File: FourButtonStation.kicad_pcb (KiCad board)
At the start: 2 copper layers, 100 x 67 mm, 39 parts, among them J1 c8-inlet, J2 Conn_WallSocket, J3 I2C, J4 AVOX Adapter, J5 Conn_WallSocket, J6 USB_B_Micro, J7 Conn_WallSocket, J8 Conn_WallSocket, J9 I2C, K1 G5Q-1, K2 G5Q-1, K4 FINDER-36.11, K5 G5Q-1, Q1 MMBT3904, Q2 MMBT3904, Q3 MMBT3904, Q4 MMBT3904, Q5 MMBT3904, Q6 MMBT3904, SW3 RST, SW4 Boot, U1 CH340C, U2 radio-receiver, U3 ESP-07

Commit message: Schematic and routing
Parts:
- removed C1: TODO: 20u as SMD Package?, Capacitor_THT:CP_Radial_D5.0mm_P2.50mm
- removed D1: TODO: SMD Diodes Package, Diode_THT:D_DO-15_P2.54mm_Vertical_KathodeUp
- removed D2, D3, D4: D_Small, Diode_THT:D_DO-15_P2.54mm_Vertical_KathodeUp
- removed K5: G5Q-1, omron-g5sb-14:RELAY_G5SB-14_OMR
- removed Q2, Q4, Q5, Q6: MMBT3904, jlc_footprints:SOT-23-3_L2.9-W1.3-P1.90-LS2.4-BR
- removed SW3: RST, jlc_footprints:SW-SMD_4P-L5.1-W5.1-P3.70-LS6.5-TL-2
- removed SW4: Boot, jlc_footprints:SW-SMD_4P-L5.1-W5.1-P3.70-LS6.5-TL-2
- added J10: AC IN, TerminalBlock_Phoenix:TerminalBlock_Phoenix_MKDS-1,5-2_1x02_P5.00mm_Horizontal, F.Cu at (117.8, 138.2)
- added K3: G5LE-1, Relay_THT:Relay_SPDT_Omron-G5LE-1, F.Cu at (60.0, 122.0)
- added LED1: KT-0603R, jlc_footprints:LED0603-RD, F.Cu at (22.3, 117.3)
- added LED2: KT-0603R, jlc_footprints:LED0603-RD, F.Cu at (39.0, 117.3)
- added LED3: KT-0603R, jlc_footprints:LED0603-RD, F.Cu at (57.0, 117.3)
- added LED4: KT-0603R, jlc_footprints:LED0603-RD, F.Cu at (73.5, 117.3)
- added R10: 33k, jlc_footprints:R0603, F.Cu at (82.7, 117.2)
- added R2: 12k, jlc_footprints:R0402, F.Cu at (37.4, 102.5)
- added R3: 12k, jlc_footprints:R0402, F.Cu at (34.1, 105.6)
- added R7: 1k, jlc_footprints:R0603, F.Cu at (58.8, 117.3)
- added R8: 33k, jlc_footprints:R0603, F.Cu at (66.2, 117.2)
- added R9: 1k, jlc_footprints:R0603, F.Cu at (75.3, 117.3)
- added SW1: POWER, as12ap:as12ap, F.Cu at (81.7, 93.7)
- added SW2: RST, jlc_footprints:SW-SMD_4P-L5.1-W5.1-P3.70-LS6.5-TL-2, F.Cu at (74.8, 96.8)
- added SWe: Mode, jlc_footprints:SW-SMD_4P-L5.1-W5.1-P3.70-LS6.5-TL-2, F.Cu at (74.8, 106.2)
- added U10: SM4007PL, jlc_footprints:SOD-123F_L2.8-W1.8-LS3.7-RD, F.Cu at (70.8, 116.8)
- added U11: D882_C9634, jlc_footprints:SOT-89-3_L4.5-W2.5-P1.50-LS4.2-BR, F.Cu at (79.6, 116.5)
- added U4: SM4007PL, jlc_footprints:SOD-123F_L2.8-W1.8-LS3.7-RD, F.Cu at (19.5, 116.8)
- added U5: D882_C9634, jlc_footprints:SOT-89-3_L4.5-W2.5-P1.50-LS4.2-BR, F.Cu at (28.4, 116.5)
- added U6: SM4007PL, jlc_footprints:SOD-123F_L2.8-W1.8-LS3.7-RD, F.Cu at (36.3, 116.8)
- added U7: D882_C9634, jlc_footprints:SOT-89-3_L4.5-W2.5-P1.50-LS4.2-BR, F.Cu at (45.1, 116.5)
- added U8: SM4007PL, jlc_footprints:SOD-123F_L2.8-W1.8-LS3.7-RD, F.Cu at (54.3, 116.8)
- added U9: D882_C9634, jlc_footprints:SOT-89-3_L4.5-W2.5-P1.50-LS4.2-BR, F.Cu at (63.1, 116.5)
- J1: value c8-inlet -> AC IN
- J2: value Conn_WallSocket -> External 3V; footprint TerminalBlock_Phoenix:TerminalBlock_Phoenix_MKDS-1,5-2_1x02_P5.00mm_Horizontal -> Connector_PinHeader_2.54mm:PinHeader_1x02_P2.54mm_Vertical
- J3: value I2C -> TTL
- J4: value AVOX Adapter -> TODO: AVOX Adapter might need voltage divider
- J6: footprint Connector_USB:USB_Micro-B_Molex-105017-0001 -> jlc_footprints:MICRO-USB-SMD_1050171001
- J9: value I2C -> Conn_WallSocket; footprint jlc_footprints:CONN-SMD_BM04B-SRSS-TB -> TerminalBlock_Phoenix:TerminalBlock_Phoenix_MKDS-1,5-2_1x02_P5.00mm_Horizontal
- K1, K2: value G5Q-1 -> G5LE-1; footprint omron-g5sb-14:RELAY_G5SB-14_OMR -> Relay_THT:Relay_SPDT_Omron-G5LE-1
- K4: value FINDER-36.11 -> G5LE-1; footprint omron-g5sb-14:RELAY_G5SB-14_OMR -> Relay_THT:Relay_SPDT_Omron-G5LE-1
- R1: footprint Resistor_SMD:R_0603_1608Metric_Pad0.98x0.95mm_HandSolder -> jlc_footprints:R0603
- R4, R5: value TODO: 33k needs to be JLC Package -> 1k; footprint Resistor_SMD:R_0603_1608Metric_Pad0.98x0.95mm_HandSolder -> jlc_footprints:R0603
- R6: value TODO: 33k needs to be JLC Package -> 33k; footprint Resistor_SMD:R_0603_1608Metric_Pad0.98x0.95mm_HandSolder -> jlc_footprints:R0603
- moved R4 204.3 mm to (24.0, 117.3), turned to 90 degrees
- moved H4 193.3 mm to (21.1, 94.5)
- moved R5 187.9 mm to (40.8, 117.3), turned to 90 degrees
- moved H3 186.0 mm to (21.2, 148.2)
- moved R6 180.0 mm to (48.2, 117.2), turned to -90 degrees
- moved R1 161.7 mm to (31.5, 117.2), turned to -90 degrees
- moved J4 127.2 mm to (68.2, 95.7)
- moved Q3 113.5 mm to (35.0, 102.3), turned to -90 degrees
- moved Q1 113.2 mm to (36.5, 105.8), turned to 90 degrees
- moved H2 96.1 mm to (117.8, 94.8)
- moved J9 88.3 mm to (72.2, 148.1)
- moved U2 73.3 mm to (87.0, 91.3)
- moved K1 62.4 mm to (26.0, 122.0)
- moved PS1 55.5 mm to (97.0, 140.0), turned to 90 degrees
- moved J5 45.2 mm to (29.8, 148.1)
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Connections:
- J2 pad 1: /AC2 -> GND
- J2 pad 2: /Nullleiter -> POWX
- J3 pad 2: +3V3 -> TX
- J3 pad 3: SDA -> RX
- J3 pad 4: SCL -> +3V3
- J4 pad 1: +3V3 -> GND
- J4 pad 2: GND -> ADC
- J4 pad 3: ADC -> +3V3
- J7 pad 1: /AC3 -> /AC2
- J8 pad 1: /AC4 -> /AC3
- J9 pad 1: GND -> /AC4
- J9 pad 2: +3V3 -> /Nullleiter
- K1 pad 1: Net-(D1-A) -> /Phase
- K1 pad 2: /Phase -> Net-(U4-A)
- K2 pad 1: Net-(D3-A) -> /Phase
- K2 pad 2: /Phase -> Net-(U6-A)
- K2 pad 3: /AC3 -> /AC2
- K4 pad 1: (no net) -> /Phase
- K4 pad 2: (no net) -> Net-(U10-A)
- K4 pad 3: (no net) -> /AC4
- K4 pad 4: (no net) -> unconnected-(K4-Pad4)
- PS1 pad 4: +3V3 -> Net-(PS1-+Vo)
- R4 pad 1: Relay2 -> Net-(U4-A)
- R5 pad 1: Relay3 -> Net-(U6-A)
- R6 pad 1: Relay4 -> Relay2
- U3 pad 1: Net-(U3-~{RST}) -> RESET
- U3 pad 10: SCL -> RadioC
- U3 pad 11: RadioD -> RadioB
- U3 pad 12: Net-(U3-GPIO0) -> GPIO0
- U3 pad 13: RadioC -> RadioA
- U3 pad 15: TX -> RX
- U3 pad 16: RX -> TX
- U3 pad 7: SDA -> RadioD
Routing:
- net /Phase: track 0.00 -> 207.1 mm
- net /Nullleiter: track 0.00 -> 109.4 mm
- net RadioD: track 0.00 -> 70.6 mm, vias 0 -> 2
- net RESET: track 0.00 -> 57.3 mm, vias 0 -> 3
- net RadioB: track 0.00 -> 56.8 mm, vias 0 -> 2
- net RadioC: track 0.00 -> 56.1 mm, vias 0 -> 2
- net RadioA: track 0.00 -> 55.3 mm, vias 0 -> 2
- net GPIO0: track 0.00 -> 50.7 mm, vias 0 -> 4
- net Relay4: track 0.00 -> 49.9 mm, vias 0 -> 2
- net RX: track 0.00 -> 45.4 mm, vias 0 -> 2
- net TX: track 0.00 -> 44.9 mm, vias 0 -> 2
- net +3V3: track 0.00 -> 42.8 mm
- net Relay3: track 0.00 -> 36.3 mm, vias 0 -> 2
- net /AC_FUSE: track 0.00 -> 31.7 mm
- net GND: track 0.00 -> 27.8 mm, vias 0 -> 10
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- added copper zone on F.Cu, net +3V3
- added copper zone on B.Cu, net GND
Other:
- board size 100 x 67 mm -> 106 x 63.5 mm

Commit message: Prepare for production
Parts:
- removed SWe: Mode, jlc_footprints:SW-SMD_4P-L5.1-W5.1-P3.70-LS6.5-TL-2
- added C1: 10u, jlc_footprints:C0402, F.Cu at (29.8, 93.5)
- added C2: 100n, jlc_footprints:C0402, F.Cu at (28.4, 93.5)
- added C3: 22u, jlc_footprints:C0603, F.Cu at (26.9, 93.5)
- added C4: 100u, jlc_footprints:C1206, F.Cu at (28.6, 112.0)
- added C5: 100n, jlc_footprints:C0402, F.Cu at (39.1, 111.5)
- added C6: 10u, jlc_footprints:C0402, F.Cu at (38.0, 111.5)
- added R11: 22k, jlc_footprints:R0603, F.Cu at (70.0, 106.0)
- added R12: 10k, jlc_footprints:R0603, F.Cu at (70.0, 108.0)
- added SW5: Mode, jlc_footprints:SW-SMD_4P-L5.1-W5.1-P3.70-LS6.5-TL-2, F.Cu at (74.8, 105.0)
- added SYM1: SYM_Flash_XLarge, Symbol:Symbol_HighVoltage_Type2_CopperTop_VerySmall, B.Cu at (101.0, 129.5)
- added Sym2: github.com/besi/four-button-station, Symbol:OSHW-Symbol_6.7x6mm_SilkScreen, F.Cu at (64.5, 108.8)
- added U13: AMS1117-3_3, jlc_footprints:SOT-223-3_L6.5-W3.4-P2.30-LS7.0-BR, F.Cu at (33.7, 96.2)
- added kibuzzard-65EDF79E: G***, kibuzzard-65EDF79E, F.Cu at (117.0, 107.0)
- added kibuzzard-65EDF7BF: G***, kibuzzard-65EDF7BF, F.Cu at (95.0, 93.3)
- added kibuzzard-65EE2541: G***, kibuzzard-65EE2541, F.Cu at (58.0, 114.5)
- added kibuzzard-65EE2549: G***, kibuzzard-65EE2549, F.Cu at (39.5, 153.2)
- added kibuzzard-65EE2549: G***, kibuzzard-65EE2549, F.Cu at (40.0, 114.5)
- added kibuzzard-65EE2550: G***, kibuzzard-65EE2550, F.Cu at (25.0, 153.2)
- added kibuzzard-65EE2550: G***, kibuzzard-65EE2550, F.Cu at (23.0, 114.5)
- added kibuzzard-65EE2558: G***, kibuzzard-65EE2558, F.Cu at (74.5, 114.5)
- added kibuzzard-65EE261E: G***, kibuzzard-65EE261E, F.Cu at (82.8, 91.5)
- added kibuzzard-65EE2681: G***, kibuzzard-65EE2681, F.Cu at (81.2, 109.2)
- added kibuzzard-65EE2746: G***, kibuzzard-65EE2746, F.Cu at (66.0, 100.1)
- added kibuzzard-65EE278E: G***, kibuzzard-65EE278E, F.Cu at (117.5, 144.2)
- added kibuzzard-65EE27C8: G***, kibuzzard-65EE27C8, F.Cu at (82.0, 153.2)
- added kibuzzard-65EE27E0: G***, kibuzzard-65EE27E0, F.Cu at (67.2, 153.2)
- added kibuzzard-65EE2811: G***, kibuzzard-65EE2811, F.Cu at (22.2, 144.8)
- added kibuzzard-65EE298C: G***, kibuzzard-65EE298C, F.Cu at (83.5, 107.2)
- added kibuzzard-65EE35B8: G***, kibuzzard-65EE35B8, F.Cu at (71.0, 100.2)
- J3: value TTL -> UART
- J4: value TODO: AVOX Adapter might need voltage divider -> ADC
- moved H3 2.50 mm to (21.2, 150.8)
- moved J4 1.99 mm to (68.8, 97.6)
- moved J7 1.90 mm to (44.5, 149.8)
- moved J8 1.90 mm to (57.5, 149.8)
- moved SW1 1.85 mm to (81.7, 95.5)
- moved H2 1.80 mm to (119.2, 93.8)
- moved J9 1.75 mm to (72.2, 149.8)
- moved J5 1.66 mm to (29.8, 149.8)
- moved J3 1.62 mm to (63.8, 96.2)
- moved J2 1.60 mm to (81.2, 104.8)
- moved SW2 1.30 mm to (74.8, 95.5)
- moved H1 1.00 mm to (119.2, 150.8)
- moved H4 0.73 mm to (21.2, 93.8)
- moved J6 0.53 mm to (20.2, 103.2)
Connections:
- net POWX renamed POW3V3
- J10 pad 1: /Nullleiter -> /AC_FUSE
- J4 pad 2: ADC -> Net-(J4-Pin_2)
- J6 pad 1: VBUS -> +5V
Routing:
- net POW3V3: track 5.31 -> 68.4 mm, vias 0 -> 2
- net /Nullleiter: track 109.4 -> 89.3 mm
- net GND: track 27.8 -> 45.4 mm, vias 10 -> 21
- net TX: track 44.9 -> 54.4 mm, vias 2 -> 1
- net +3V3: track 42.8 -> 51.7 mm
- net RX: track 45.4 -> 54.0 mm, vias 2 -> 1
- net ADC: track 27.4 -> 34.4 mm, vias 1 -> 2
- net Net-(J4-Pin_2): track 0.00 -> 6.69 mm
- net +5V: track 0.00 -> 4.60 mm
- net Relay3: track 36.3 -> 40.6 mm
- net /Phase: track 207.1 -> 203.5 mm
- net /AC_FUSE: track 31.7 -> 35.1 mm
- net /AC1: track 15.9 -> 17.6 mm
- net RESET: track 57.3 -> 58.8 mm
- net /AC4: track 12.8 -> 14.2 mm
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- added copper zone on F.Cu, net +5V
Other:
- board size 106 x 63.5 mm -> 106 x 65 mm
- board text added: "JLCJLCJLCJLC"
- board text added: "Version 2.0 10.03.24 aabbccdd"

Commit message: Final tweaks
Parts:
- moved F1 1.42 mm to (110.0, 149.8)
- moved PS1 0.77 mm to (97.0, 140.8)
- moved SW2 0.75 mm to (74.8, 96.2)
- moved kibuzzard-65EDF7BF 0.66 mm to (95.0, 94.0)
- moved U2 0.65 mm to (87.0, 92.0)
- moved J10 0.50 mm to (117.2, 138.2)
- moved J1 0.25 mm to (120.0, 120.2)
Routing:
- net /AC_FUSE: track 35.1 -> 32.4 mm
- net GND: track 45.4 -> 44.2 mm
- net RESET: track 58.8 -> 58.0 mm
- net RadioD: track 71.4 -> 70.8 mm
- net RadioC: track 56.3 -> 55.6 mm
- net +3V3: track 51.7 -> 51.0 mm
- net RadioB: track 56.9 -> 56.2 mm
- net /Nullleiter: track 89.3 -> 88.7 mm
- net /Phase: track 203.5 -> 202.9 mm

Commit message: Production files for 2.0
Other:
- board text added: "Version 2.0 10.03.24 aa14c0f4"
- board text removed: "Version 2.0 10.03.24 aabbccdd"
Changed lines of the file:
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@@
   (gr_line (start 37.25 91.75) (end 37.25 94.75)
     (stroke (width 0.1) (type default)) (layer "Edge.Cuts"))
-  (gr_text "Version 2.0\n10.03.24\naabbccdd" (at 113 104) (layer "F.SilkS")
+  (gr_text "Version 2.0\n10.03.24\naa14c0f4" (at 113 104) (layer "F.SilkS")
     (effects (font (size 1 1) (thickness 0.15)) (justify left bottom))
   )

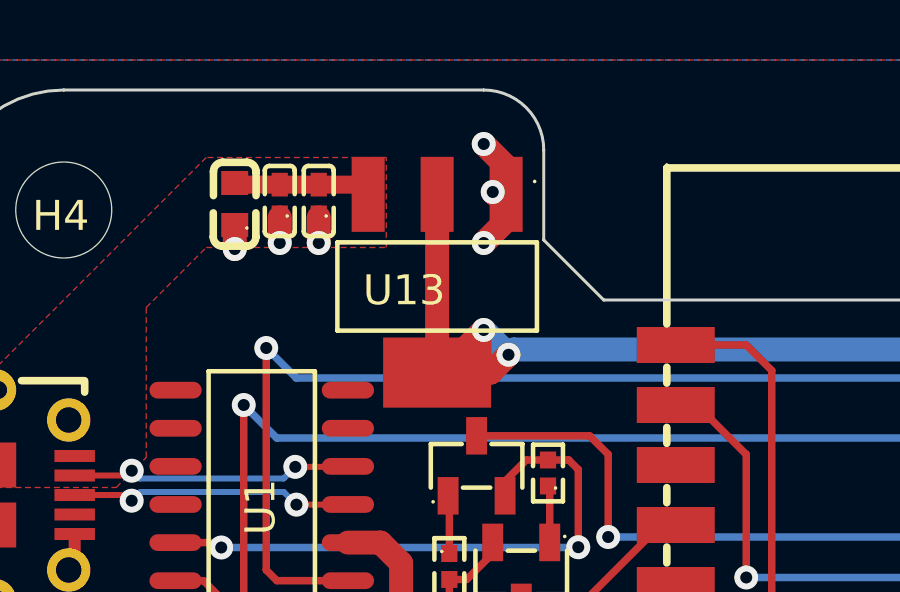
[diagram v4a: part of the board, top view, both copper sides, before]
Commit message: Thermal conductivity for the AMS117
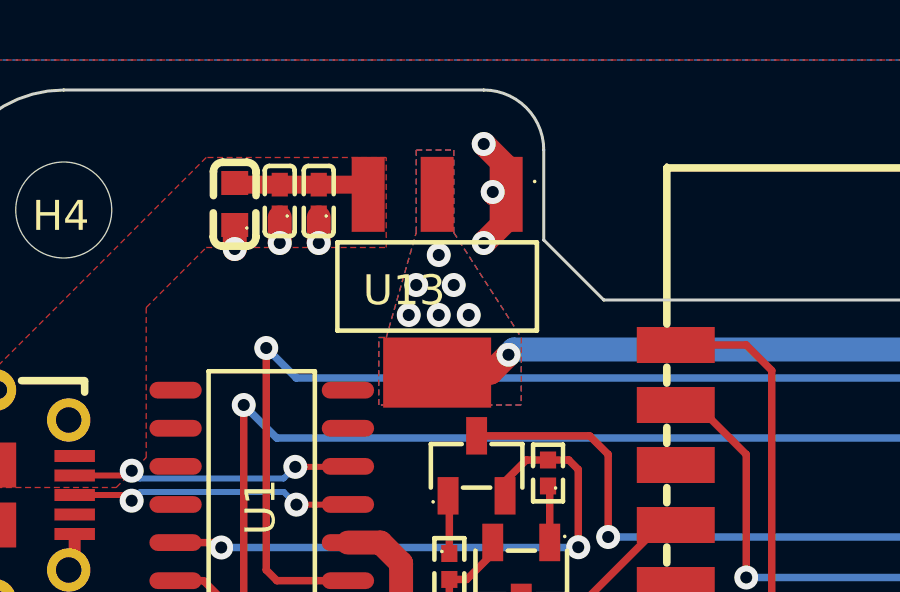
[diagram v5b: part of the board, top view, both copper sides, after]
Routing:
- net POW3V3: track 68.4 -> 59.3 mm, vias 2 -> 7
- added copper zone on B.Cu, net POW3V3
- added copper zone on F.Cu, net POW3V3
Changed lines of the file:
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@@
   (segment (start 83.75 104.71) (end 83.79 104.75) (width 0.8) (layer "F.Cu") (net 61))
   (segment (start 35.480949 99.169051) (end 36.075 98.575) (width 0.8) (layer "F.Cu") (net 61))
-  (segment (start 33.697116 93.229122) (end 33.697116 99.169051) (width 0.8) (layer "F.Cu") (net 61))
   (segment (start 82.83 100.58) (end 83.75 101.5) (width 0.8) (layer "F.Cu") (net 61))
-  (segment (start 33.830949 99.169051) (end 35.25 97.75) (width 0.8) (layer "F.Cu") (net 61))
   (segment (start 33.697116 99.169051) (end 35.480949 99.169051) (width 0.8) (layer "F.Cu") (net 61))
+  (via (at 33 96.25) (size 0.8) (drill 0.4) (layers "F.Cu" "B.Cu") (free) (net 61))
+  (via (at 33.75 97.25) (size 0.8) (drill 0.4) (layers "F.Cu" "B.Cu") (free) (net 61))
   (via (at 36.075 98.575) (size 0.8) (drill 0.4) (layers "F.Cu" "B.Cu") (net 61))
-  (via (at 35.25 97.75) (size 0.8) (drill 0.4) (layers "F.Cu" "B.Cu") (net 61))
+  (via (at 34.25 96.25) (size 0.8) (drill 0.4) (layers "F.Cu" "B.Cu") (free) (net 61))
+  (via (at 34.75 97.25) (size 0.8) (drill 0.4) (layers "F.Cu" "B.Cu") (free) (net 61))
+  (via (at 32.75 97.25) (size 0.8) (drill 0.4) (layers "F.Cu" "B.Cu") (free) (net 61))
+  (via (at 33.75 95.25) (size 0.8) (drill 0.4) (layers "F.Cu" "B.Cu") (free) (net 61))
   (segment (start 36.250001 98.399999) (end 36.075 98.575) (width 0.8) (layer "B.Cu") (net 61))
-  (segment (start 35.25 97.75) (end 36.075 98.575) (width 0.8) (layer "B.Cu") (net 61))
   (segment (start 60.518127 98.399999) (end 36.250001 98.399999) (width 0.8) (layer "B.Cu") (net 61))
   (segment (start 81.65 100.58) (end 78.58 100.58) (width 0.8) (layer "B.Cu") (net 61))
@@
   )
   (zone (net 59) (net_name "+5V") (layer "F.Cu") (name "5v") (hatch edge 0.5)
-    (priority 1)
+    (priority 3)
     (connect_pads yes (clearance 0.25))
     (min_thickness 0.25) (filled_areas_thickness no)
@@
     )
   )
+  (zone (net 0) (net_name "") (layers "F&B.Cu") (name "Keepout-antenna-zone") (hatch edge 0.5)
+    (connect_pads yes (clearance 0))
+    (min_thickness 0.25) (filled_areas_thickness no)
+    (keepout (tracks allowed) (vias allowed) (pads allowed) (copperpour not_allowed) (footprints allowed))
+    (fill (thermal_gap 0.5) (thermal_bridge_width 0.5))
+    (polygon
+      (pts
+        (xy 37.25 89.75)
+        (xy 37.25 97.75)
+        (xy 61.25 97.75)
+        (xy 61.25 89.75)
+      )
+    )
+  )
+  (zone (net 61) (net_name "POW3V3") (layers "F&B.Cu") (hatch edge 0.5)
+    (priority 4)
+    (connect_pads (clearance 0))
+    (min_thickness 0.25) (filled_areas_thickness no)
+    (fill yes (thermal_gap 0.1) (thermal_bridge_width 0.8))
+    (polygon
+      (pts
+        (xy 32 98)
+        (xy 33 94.5)
+        (xy 33 91.75)
+        (xy 34.25 91.75)
+        (xy 34.25 94.5)
+        (xy 36.5 98)
+        (xy 36.5 100.25)
+        (xy 31.75 100.25)
+        (xy 31.75 98)
+      )
+    )
+  )
   (zone (net 1) (net_name "GND") (layer "B.Cu") (hatch edge 0.5)
     (priority 2)
@@
         (xy 111.25 88.75)
         (xy 13.25 88.75)
-        (xy 13.25 115.5)
       )
     )

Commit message: Prepare release 2.0
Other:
- board text added: "Version 2.0 11.03.24 95fb5d44"
- board text removed: "Version 2.0 10.03.24 aa14c0f4"
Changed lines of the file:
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@@
   (gr_line (start 37.25 91.75) (end 37.25 94.75)
     (stroke (width 0.1) (type default)) (layer "Edge.Cuts"))
-  (gr_text "Version 2.0\n10.03.24\naa14c0f4" (at 113 104) (layer "F.SilkS")
+  (gr_text "Version 2.0\n11.03.24\n95fb5d44" (at 113 104) (layer "F.SilkS")
     (effects (font (size 1 1) (thickness 0.15)) (justify left bottom))
   )

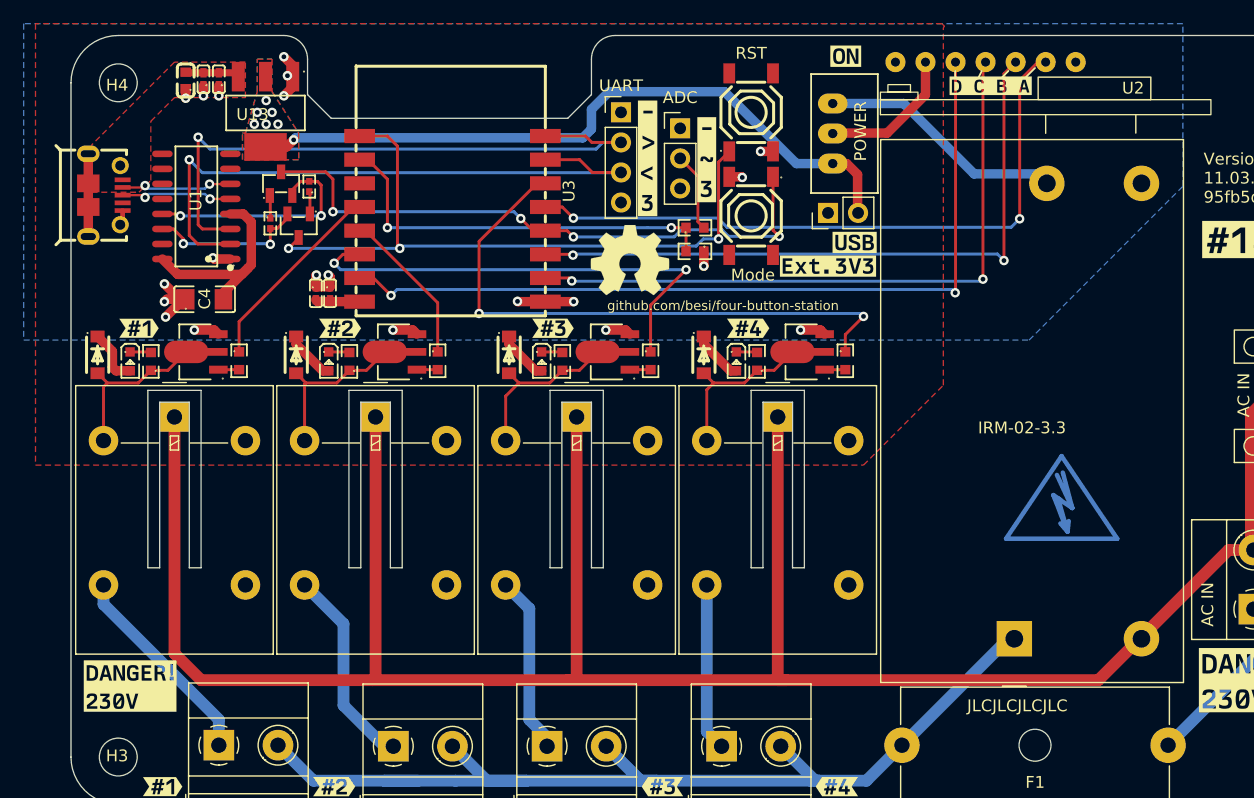
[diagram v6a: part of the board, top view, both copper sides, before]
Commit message: Update documentation and silkscreen
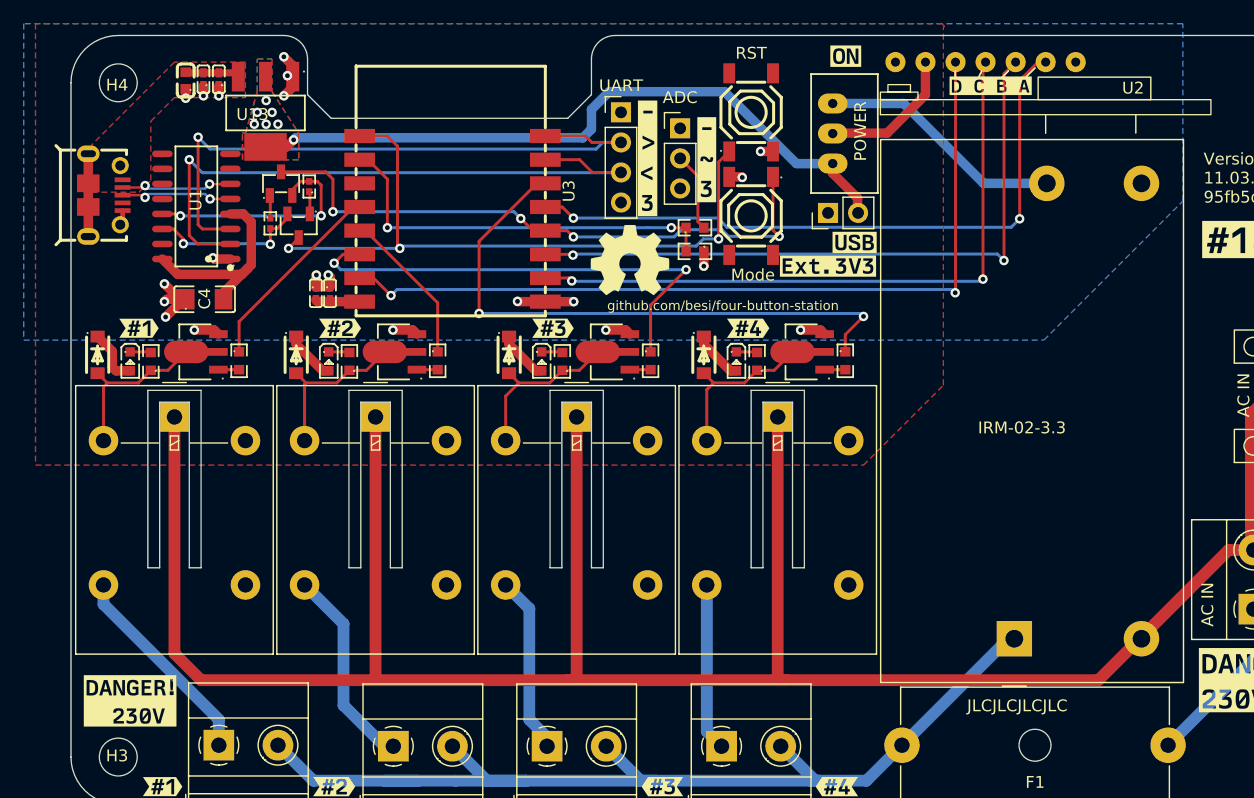
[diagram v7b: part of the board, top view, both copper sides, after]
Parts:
- removed the SYM1 at (101.0, 129.5)
- removed kibuzzard-65EE2811: G***, kibuzzard-65EE2811
- added G*** (x2): LOGO, LOGO, B.Cu at (76.8, 105.2)
- added G***: LOGO, LOGO, B.Cu at (29.8, 102.8)
- added SYM1: SYM_Flash_XLarge, Symbol:Symbol_HighVoltage_Type2_CopperTop_VerySmall, B.Cu at (43.0, 143.0)
- added SYM1: SYM_Flash_XLarge, Symbol:Symbol_HighVoltage_Type2_CopperTop_VerySmall, B.Cu at (109.5, 133.0)
- added SYM1: SYM_Flash_XLarge, Symbol:Symbol_HighVoltage_Type2_CopperTop_VerySmall, B.Cu at (77.0, 143.0)
- added SYM1: SYM_Flash_XLarge, Symbol:Symbol_HighVoltage_Type2_CopperTop_VerySmall, B.Cu at (109.5, 119.8)
- added SYM1: SYM_Flash_XLarge, Symbol:Symbol_HighVoltage_Type2_CopperTop_VerySmall, B.Cu at (26.0, 143.0)
- added SYM1: SYM_Flash_XLarge, Symbol:Symbol_HighVoltage_Type2_CopperTop_VerySmall, B.Cu at (102.8, 143.0)
- added SYM1: SYM_Flash_XLarge, Symbol:Symbol_HighVoltage_Type2_CopperTop_VerySmall, B.Cu at (60.0, 143.0)
- added Sym2: github.com/besi/four-button-station, Symbol:OSHW-Symbol_6.7x6mm_SilkScreen, B.Cu at (40.5, 105.8)
- added kibuzzard-65F05324: G***, kibuzzard-65F05324, F.Cu at (22.2, 146.0)
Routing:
- net POW3V3: track 59.3 -> 58.6 mm

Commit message: Update version
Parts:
- removed the G*** at (76.8, 105.2)
- added Logo1: github.com/besi/four-button-station, Symbol:OSHW-Symbol_6.7x6mm_SilkScreen, F.Cu at (64.5, 108.8)
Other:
- board text added: "Version 2.0 11.03.24 38dd1e96"
- board text removed: "Version 2.0 11.03.24 95fb5d44"
